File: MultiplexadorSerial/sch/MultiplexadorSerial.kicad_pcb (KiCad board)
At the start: 2 copper layers, 54.5 x 69.5 mm, 57 parts, among them Q1 Q_NPN_CBE, Q2 Q_NPN_CBE, Q3 Q_NPN_CBE, Q4 Q_NPN_CBE, U1 SP3481CP, U2 SP3481CP, U3 SP3481CP, U4 SP3481CP, U5 4052

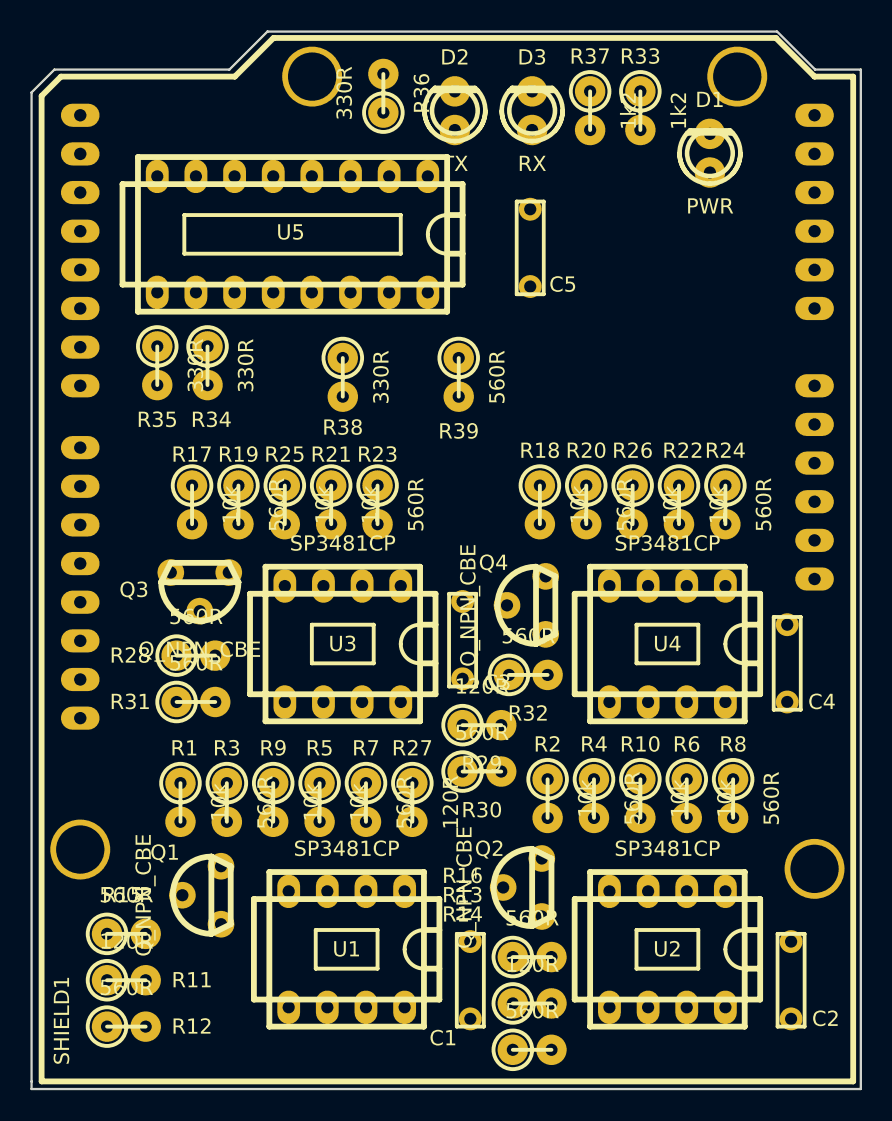
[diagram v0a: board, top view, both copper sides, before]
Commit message: Multiplexador Serial RS485 arduino
Signed-off-by: cuki2 <mauricio@krebs.com.br>
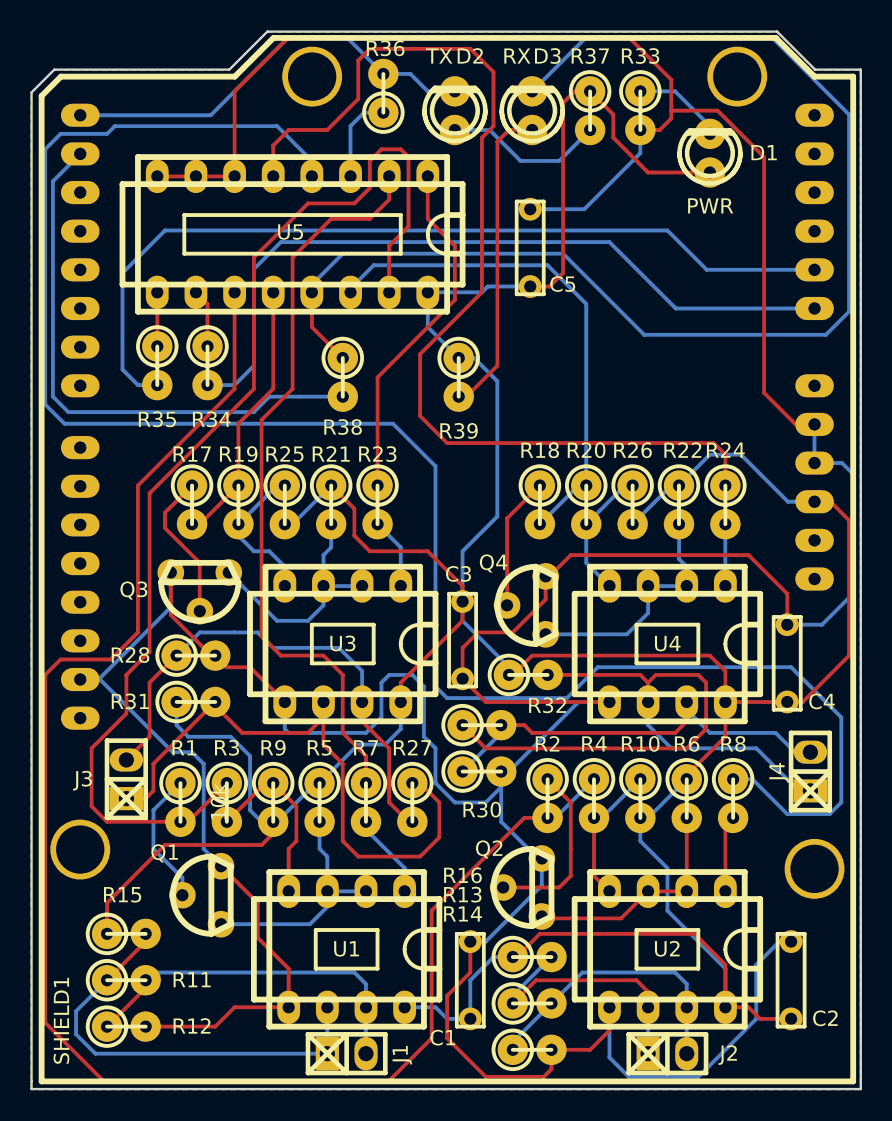
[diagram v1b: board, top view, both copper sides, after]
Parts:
- added J1: SL4, w_pin_strip:pin_socket_2, F.Cu at (76.7, 138.2)
- added J2: SL3, w_pin_strip:pin_socket_2, F.Cu at (97.8, 138.2)
- added J3: SL1, w_pin_strip:pin_socket_2, F.Cu at (62.2, 120.1)
- added J4: SL2, w_pin_strip:pin_socket_2, F.Cu at (107.2, 119.6)
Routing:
- net GND: track 0.00 -> 298.7 mm
- net VDD: track 0.00 -> 242.1 mm
- net Net-(R8-Pad1): track 0.00 -> 121.9 mm
- net Net-(R2-Pad2): track 0.00 -> 106.4 mm
- net Net-(D3-Pad2): track 0.00 -> 82.0 mm
- net Net-(R1-Pad2): track 0.00 -> 74.6 mm
- net Net-(R24-Pad1): track 0.00 -> 69.0 mm
- net Net-(R35-Pad2): track 0.00 -> 56.8 mm
- net Net-(R34-Pad2): track 0.00 -> 49.3 mm
- net Net-(R7-Pad1): track 0.00 -> 49.3 mm
- net Net-(J4-Pad1): track 0.00 -> 46.5 mm
- net Net-(J3-Pad1): track 0.00 -> 40.6 mm
- net Net-(R38-Pad2): track 0.00 -> 36.6 mm
- net Net-(R18-Pad2): track 0.00 -> 34.5 mm
- net Net-(J3-Pad2): track 0.00 -> 33.5 mm
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- added copper zone on B.Cu, net GND
- added copper zone on F.Cu, net GND
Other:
- net class Default: clearance 0.2 -> 0.1
- rule trace_clearance: 0.2 -> 0.1

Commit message: Bottom
Signed-off-by: cuki2 <mauricio@krebs.com.br>
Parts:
- moved R30 0.51 mm to (86.1, 119.6)
- moved R35 0.25 mm to (64.0, 93.0)
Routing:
- net GND: track 298.7 -> 1.02 mm
- net Net-(R7-Pad1): track 49.3 -> 0.00 mm
- net Net-(R1-Pad2): track 74.6 -> 122.7 mm
- net Net-(D3-Pad2): track 82.0 -> 43.2 mm
- net Net-(R2-Pad2): track 106.4 -> 71.9 mm
- net Net-(R18-Pad2): track 34.5 -> 4.10 mm
- net VDD: track 242.1 -> 270.6 mm
- net Net-(R23-Pad1): track 23.2 -> 0.00 mm
- net Net-(R8-Pad1): track 121.9 -> 100.4 mm
- net Net-(D3-Pad1): track 20.7 -> 0.00 mm
- net Net-(R17-Pad2): track 17.7 -> 38.4 mm
- net Net-(J3-Pad1): track 40.6 -> 30.9 mm
- net Net-(R38-Pad2): track 36.6 -> 27.6 mm
- net Net-(Q1-Pad2): track 8.89 -> 0.00 mm
- net Net-(J1-Pad1): track 28.6 -> 21.7 mm
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
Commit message: Multiplexador Serial
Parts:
- moved R37 4.83 mm to (87.9, 76.2)
- moved D3 3.05 mm to (91.9, 76.2)
- turned R17 to 90 degrees
- turned R18 to 90 degrees
- turned R25 to 90 degrees
- turned R26 to 90 degrees
- turned R33 to 90 degrees
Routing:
- net VDD: track 270.6 -> 79.2 mm
- net Net-(R1-Pad2): track 122.7 -> 0.00 mm
- net Net-(R8-Pad1): track 100.4 -> 0.00 mm
- net Net-(R24-Pad1): track 73.2 -> 0.00 mm
- net Net-(R2-Pad2): track 71.9 -> 0.00 mm
- net Net-(J4-Pad1): track 42.5 -> 0.00 mm
- net Net-(R34-Pad2): track 45.3 -> 76.9 mm
- net Net-(J3-Pad1): track 30.9 -> 0.00 mm
- net Net-(J4-Pad2): track 28.9 -> 0.00 mm
- net Net-(J1-Pad2): track 27.6 -> 0.00 mm
- net Net-(J3-Pad2): track 35.5 -> 8.97 mm
- net Net-(J2-Pad1): track 23.6 -> 0.00 mm
- net Net-(D3-Pad1): track 0.00 -> 22.0 mm
- net Net-(J1-Pad1): track 21.7 -> 0.00 mm
- net Net-(J2-Pad2): track 18.2 -> 0.00 mm
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- removed copper zone on F.Cu, net GND
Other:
- net class Default: clearance 0.1 -> 0.2; trace_width 0.25 -> 0.4
- rule trace_clearance: 0.1 -> 0.2

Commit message: Trilas
Signed-off-by: cuki2 <mauricio@krebs.com.br>
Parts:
- moved D1 1.37 mm to (101.1, 80.3)
- moved R30 0.57 mm to (85.6, 119.9), turned to 180 degrees
- turned R1 to 90 degrees
- turned R10 to 90 degrees
- turned R11 to 180 degrees
- turned R13 to 180 degrees
- turned R9 to 90 degrees
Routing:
- net VDD: track 79.2 -> 267.9 mm
- net Net-(R8-Pad1): track 0.00 -> 63.8 mm
- net Net-(R2-Pad2): track 0.00 -> 53.0 mm
- net Net-(R24-Pad1): track 0.00 -> 43.8 mm
- net Net-(J4-Pad1): track 0.00 -> 37.2 mm
- net Net-(J3-Pad1): track 0.00 -> 30.5 mm
- net Net-(R35-Pad2): track 50.3 -> 80.8 mm
- net Net-(J3-Pad2): track 8.97 -> 36.0 mm
- net Net-(J1-Pad2): track 0.00 -> 26.4 mm
- net Net-(R18-Pad2): track 0.00 -> 22.7 mm
- net Net-(J2-Pad2): track 0.00 -> 20.7 mm
- net Net-(J1-Pad1): track 0.00 -> 20.3 mm
- net Net-(R17-Pad2): track 35.1 -> 16.7 mm
- net Net-(J4-Pad2): track 0.00 -> 17.4 mm
- net Net-(Q2-Pad3): track 0.00 -> 16.8 mm
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- added copper zone on F.Cu, net GND

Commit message: adicionado resistores pull ups nos transdutores
Signed-off-by: cuki2 <mauricio@krebs.com.br>
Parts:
- added R40: 10k, w_pth_resistors:rc05_vert, F.Cu at (68.6, 135.4)
- added R41: 10k, w_pth_resistors:rc05_vert, F.Cu at (106.9, 131.6)
- added R42: 10k, w_pth_resistors:rc05_vert, F.Cu at (82.0, 102.1)
- added R43: 10k, w_pth_resistors:rc05_vert, F.Cu at (108.2, 111.5)
- moved C2 4.83 mm to (106.2, 138.2), turned to 0 degrees
- moved R8 1.02 mm to (103.1, 121.4)
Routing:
- net Net-(R1-Pad2): track 3.05 -> 73.8 mm, vias 0 -> 1
- net VDD: track 267.9 -> 306.0 mm
- net GND: track 0.00 -> 25.3 mm
- net Net-(J4-Pad2): track 17.4 -> 38.1 mm
- net Net-(R40-Pad2): track 5.62 -> 21.2 mm
- net Net-(R24-Pad2): track 0.00 -> 12.4 mm
- net Net-(R41-Pad2): track 5.04 -> 14.0 mm
- net Net-(J3-Pad1): track 30.5 -> 36.7 mm
- net Net-(R2-Pad2): track 53.0 -> 56.6 mm
- net Net-(R23-Pad2): track 4.99 -> 8.29 mm
- net Net-(J4-Pad1): track 37.2 -> 39.0 mm
- net Net-(J1-Pad1): track 20.3 -> 21.1 mm
- net Net-(R35-Pad2): track 80.8 -> 81.3 mm

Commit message: placa em smd
Signed-off-by: cuki2 <mauricio@krebs.com.br>
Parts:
- C1, C2, C3, C4, C5: footprint w_capacitors:cnp_6mm_disc -> w_smd_cap:c_0805
- D1: footprint w_indicators:led_3mm_green -> w_smd_leds:Led_0805
- D2: footprint w_indicators:led_3mm_red -> w_smd_leds:Led_0805
- D3: footprint w_indicators:led_3mm_clear -> w_smd_leds:Led_0805
- Q1, Q3: footprint w_to:to92_3 -> w_smd_trans:sot23
- Q2, Q4: footprint w_to:to92_3 -> w_smd_resistors:r_0805
- R1, R10, R11, R12, R13, R14, R15, R16, R17, R18, R19, R2, R20, R21, R22, R23, R24, R25, R26, R27, R28, R29, R3, R30, R31, R32, R33, R34, R35, R36, R37, R38, R39, R4, R40, R41, R42, R43, R5, R6, R7, R8, R9: footprint w_pth_resistors:rc05_vert -> w_smd_resistors:r_0805
- U1, U2, U3, U4: footprint w_pth_circuits:dil_8-300_socket -> w_smd_dil:so-8
- U5: footprint w_pth_circuits:dil_16-300_socket -> w_smd_dil:so-16
- moved U4 124.5 mm to (215.6, 71.0), turned to 270 degrees
- moved J3 107.1 mm to (163.7, 85.9)
- moved R28 96.8 mm to (158.9, 82.2), turned to 270 degrees
- moved R31 95.4 mm to (158.9, 89.9), turned to 270 degrees
- moved R38 93.1 mm to (160.9, 54.6)
- moved R12 91.8 mm to (148.5, 105.0)
- moved R11 90.8 mm to (148.5, 105.0), turned to 0 degrees
- moved J1 90.4 mm to (112.1, 55.0), turned to 180 degrees
- moved R15 89.9 mm to (148.5, 105.0)
- moved R36 86.9 mm to (163.6, 54.6), turned to 270 degrees
- moved R27 85.6 mm to (158.9, 86.0)
- moved R40 85.5 mm to (148.5, 105.0), turned to 0 degrees
- moved R35 85.3 mm to (148.5, 105.0), turned to 0 degrees
- moved R1 84.4 mm to (148.5, 105.0), turned to 0 degrees
- moved Q1 83.8 mm to (148.5, 105.0), turned to 0 degrees
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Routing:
- net VDD: track 306.0 -> 0.00 mm
- net Net-(R35-Pad2): track 81.3 -> 0.00 mm
- net Net-(R34-Pad2): track 77.3 -> 0.00 mm
- net Net-(R1-Pad2): track 73.8 -> 0.00 mm, vias 1 -> 0
- net Net-(R8-Pad1): track 63.4 -> 0.00 mm
- net Net-(R2-Pad2): track 56.6 -> 0.00 mm
- net Net-(R24-Pad1): track 43.8 -> 0.00 mm
- net Net-(D3-Pad2): track 42.2 -> 0.00 mm
- net Net-(J4-Pad1): track 39.0 -> 0.00 mm
- net Net-(J4-Pad2): track 38.1 -> 0.00 mm
- net Net-(J3-Pad1): track 36.7 -> 0.00 mm
- net Net-(J3-Pad2): track 36.0 -> 0.00 mm
- net Net-(R38-Pad2): track 29.2 -> 0.00 mm
- net Net-(D2-Pad2): track 28.2 -> 0.00 mm
- net Net-(J1-Pad2): track 26.4 -> 0.00 mm
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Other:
- board size 54.5 x 69.5 mm -> 69.2 x 54 mm

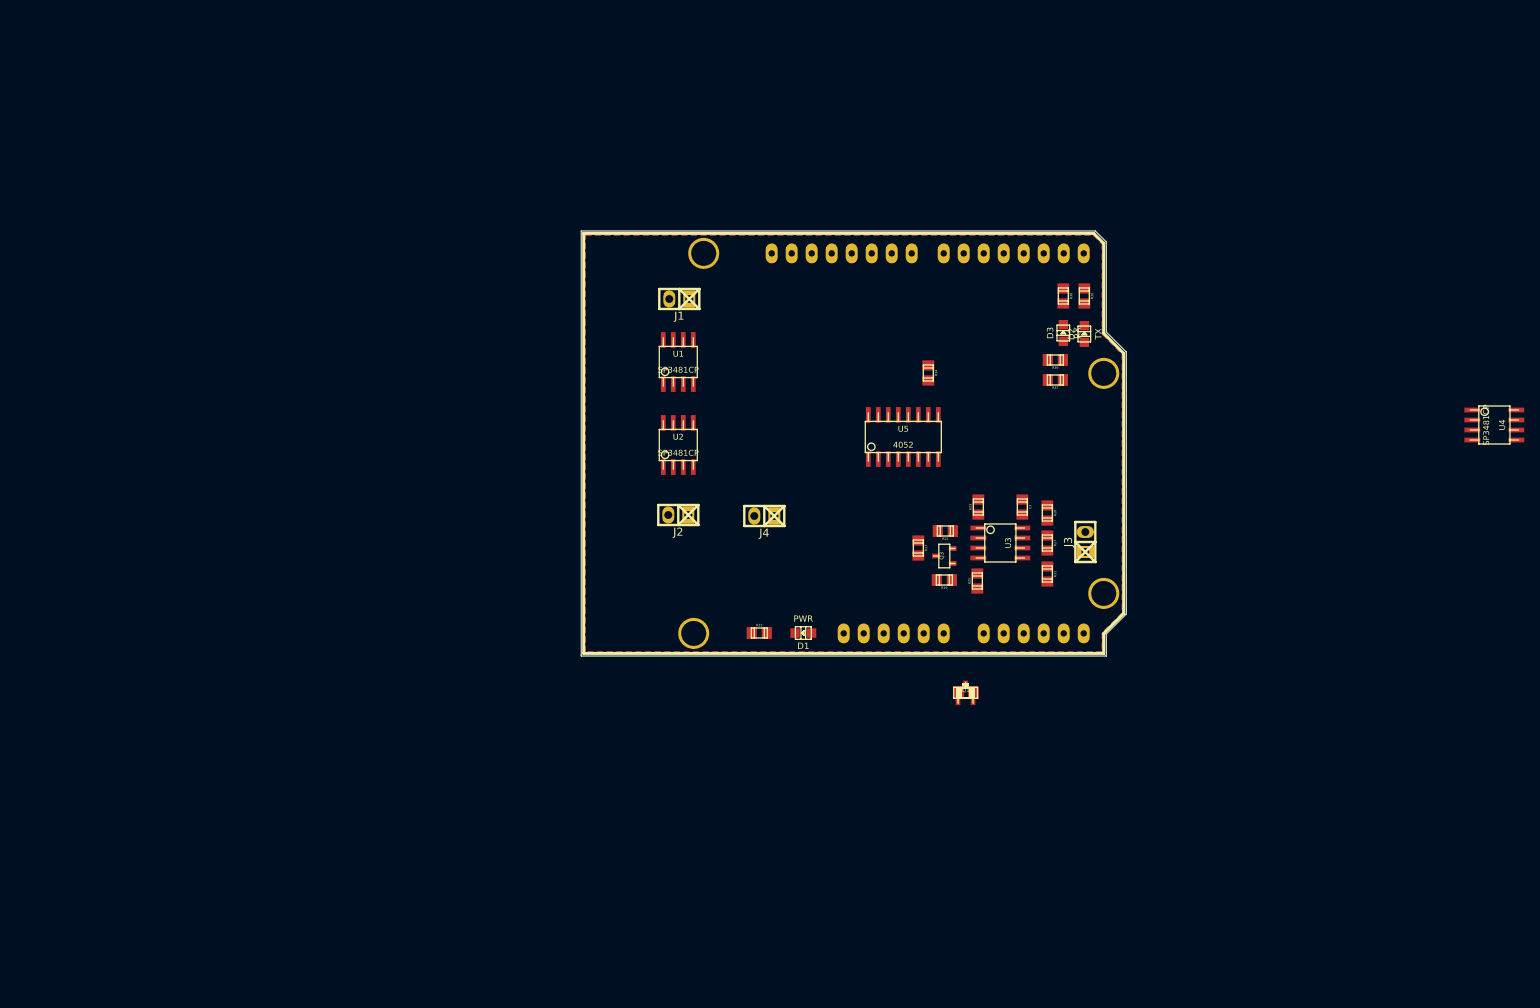
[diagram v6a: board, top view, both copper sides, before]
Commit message: posicionamento smd
Signed-off-by: cuki2 <mauricio@krebs.com.br>
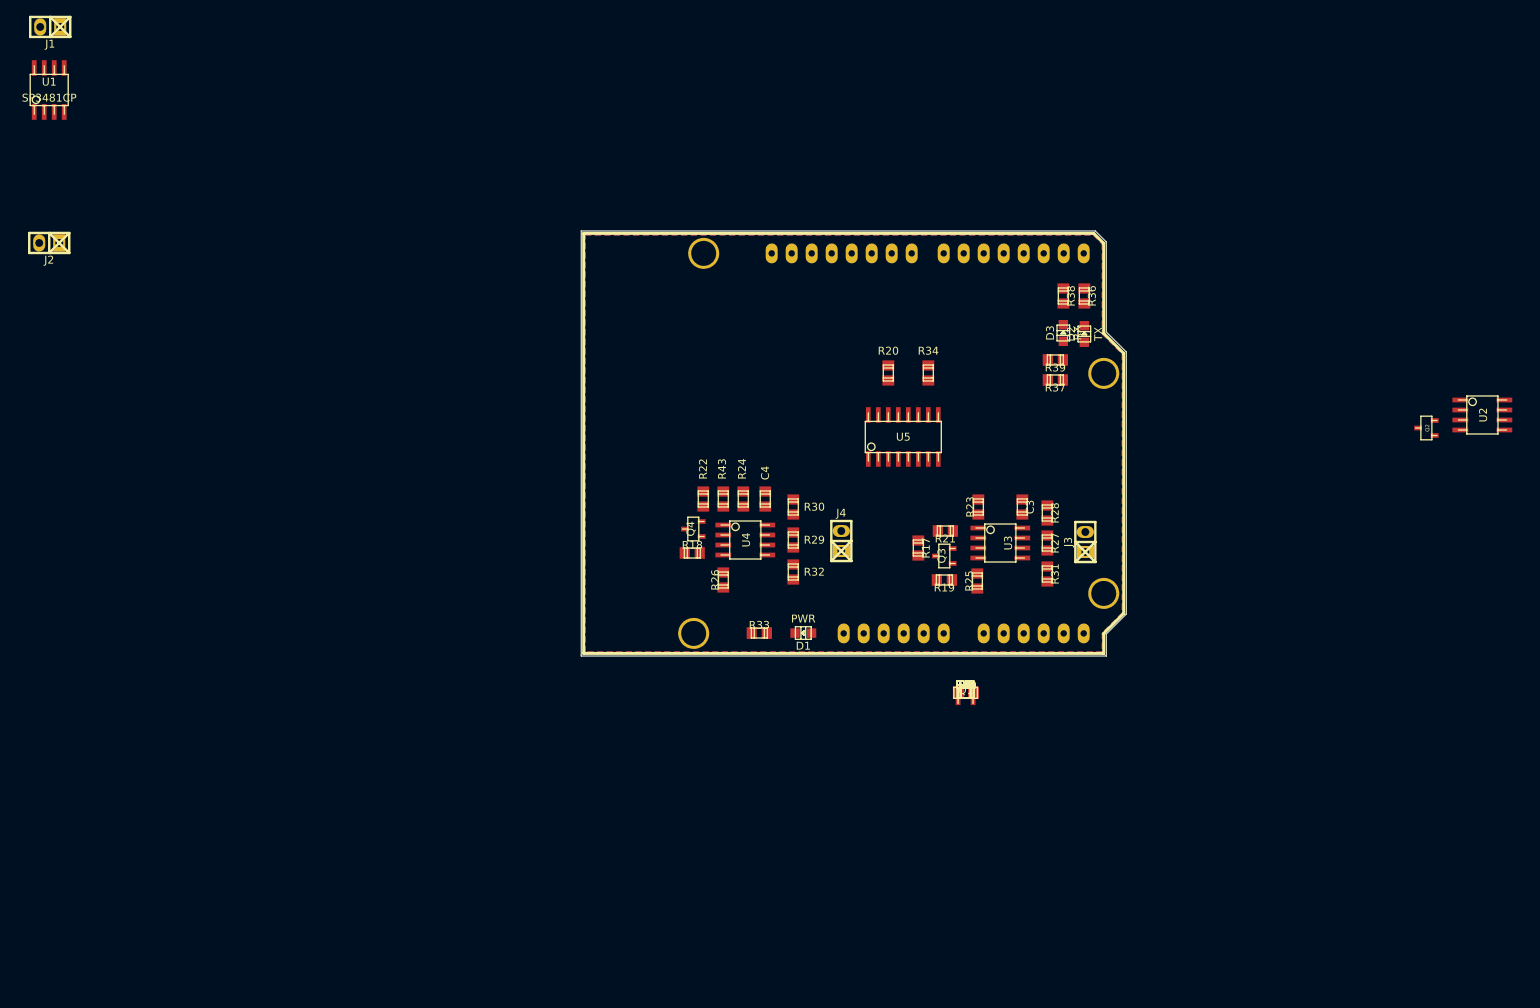
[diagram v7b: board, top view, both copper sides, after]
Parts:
- Q2, Q4: footprint w_smd_resistors:r_0805 -> w_smd_trans:sot23
- moved U2 102.2 mm to (214.1, 69.7), turned to 270 degrees
- moved U4 96.2 mm to (120.5, 85.6)
- moved J1 87.0 mm to (32.3, 20.4)
- moved J2 87.0 mm to (32.1, 47.9)
- moved U1 87.0 mm to (32.1, 28.4)
- moved Q2 67.5 mm to (207.0, 71.4), turned to 90 degrees
- moved R20 41.8 mm to (138.7, 64.4), turned to 270 degrees
- moved R22 41.4 mm to (115.2, 80.4), turned to 90 degrees
- moved Q4 40.4 mm to (113.9, 84.2), turned to 90 degrees
- moved R43 39.4 mm to (117.7, 80.4), turned to 90 degrees
- moved R18 39.0 mm to (113.8, 87.2)
- moved R24 37.5 mm to (120.3, 80.4), turned to 90 degrees
- moved C4 35.4 mm to (123.1, 80.4), turned to 270 degrees
- moved R26 33.9 mm to (117.7, 90.7), turned to 90 degrees
- moved R30 32.2 mm to (126.6, 81.4), turned to 270 degrees
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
